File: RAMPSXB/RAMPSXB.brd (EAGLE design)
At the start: 129.5 x 73.5 mm, 97 parts, among them CN1 1X4-BIG, CN2 1X4-BIG, CN3 1X4-BIG, CN4 1X4-BIG, CN5 1X4-BIG, CN6 1X4-BIG, CN7 1X4-BIG, CN8 1X4-BIG, CN9 1X4-BIG, J1 1X2-3.5MM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

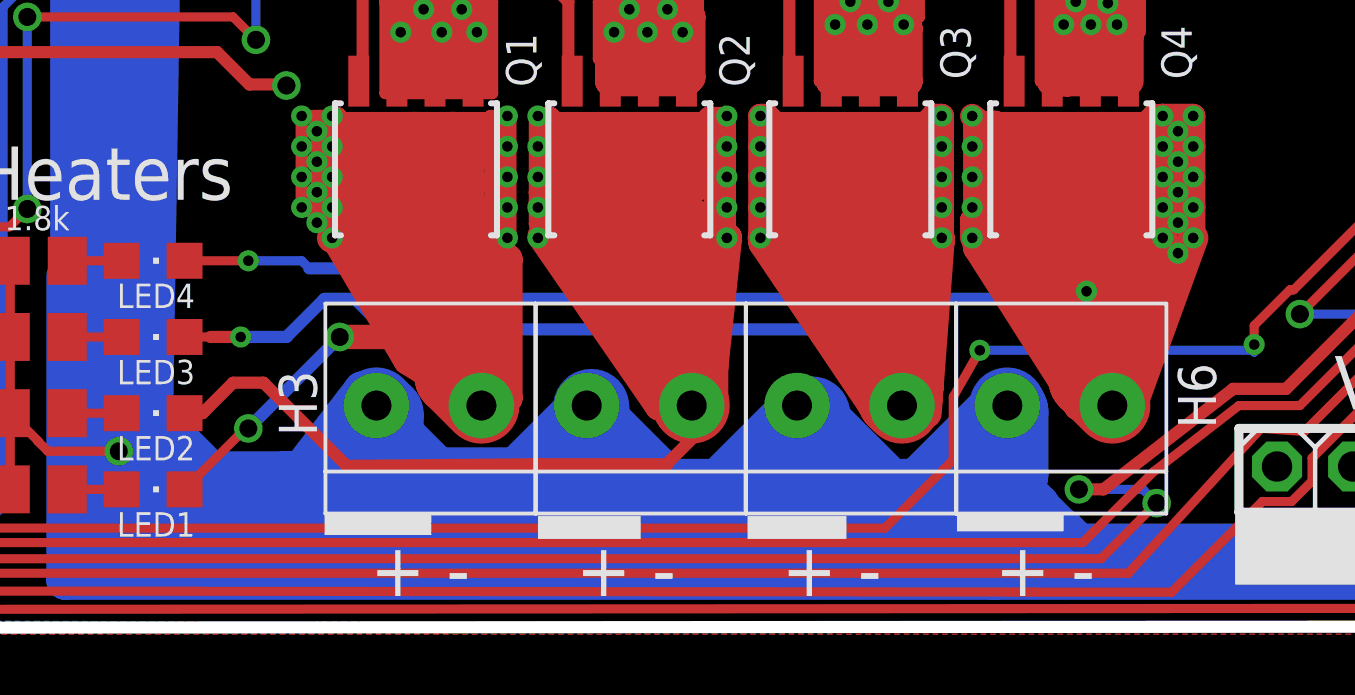
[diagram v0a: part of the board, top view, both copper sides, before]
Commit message: Added Labeling for the Heater LEDs.
So you know which one is which
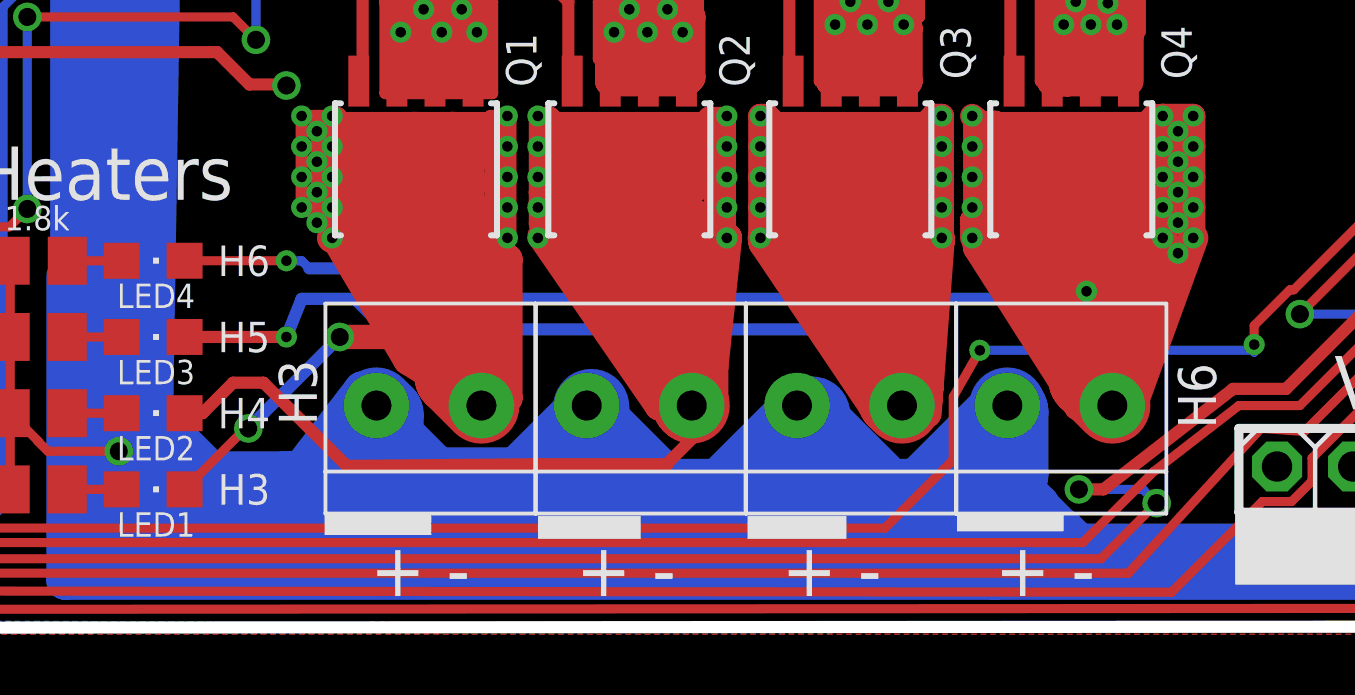
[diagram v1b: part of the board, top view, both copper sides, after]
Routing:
- net N$38: track 125.2 -> 123.6 mm
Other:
- board text added: "H4"
- board text added: "H5"
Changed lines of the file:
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@@
 <layer number="17" name="Pads" color="2" fill="1" visible="yes" active="yes"/>
 <layer number="18" name="Vias" color="2" fill="1" visible="yes" active="yes"/>
-<layer number="19" name="Unrouted" color="13" fill="1" visible="yes" active="yes"/>
+<layer number="19" name="Unrouted" color="13" fill="1" visible="no" active="yes"/>
 <layer number="20" name="Dimension" color="15" fill="1" visible="yes" active="yes"/>
 <layer number="21" name="tPlace" color="7" fill="1" visible="yes" active="yes"/>
@@
 <rectangle x1="1.9304" y1="50.292" x2="19.7104" y2="52.832" layer="21"/>
 <wire x1="22.352" y1="12.954" x2="22.606" y2="13.208" width="0.3048" layer="20"/>
-<text x="41.402" y="5.588" size="1.27" layer="21" font="vector" rot="R90">H3</text>
+<text x="40.132" y="8.128" size="1.27" layer="21" font="vector" rot="R270">H3</text>
 <text x="71.374" y="5.842" size="1.27" layer="21" font="vector" rot="R90">H6</text>
 <text x="13.3604" y="42.672" size="0.8128" layer="21" font="vector">+5V</text>
@@
 <text x="77.978" y="25.654" size="1.016" layer="21" font="vector">(C) Scott Ziv</text>
 <rectangle x1="42.5704" y1="63.5" x2="45.974" y2="70.9168" layer="21"/>
+<text x="38.1" y="3.302" size="1.016" layer="21" font="vector">H3</text>
+<text x="38.1" y="5.842" size="1.016" layer="21" font="vector">H4</text>
+<text x="38.1" y="8.382" size="1.016" layer="21" font="vector">H5</text>
+<text x="38.1" y="10.922" size="1.016" layer="21" font="vector">H6</text>
 </plain>
 <attributes>
@@
 <contactref element="J4" pad="1"/>
 <contactref element="LED3" pad="C"/>
-<wire x1="36.991" y1="8.89" x2="37.846" y2="8.89" width="0.3048" layer="1"/>
+<wire x1="36.991" y1="8.89" x2="37.338" y2="8.89" width="0.3048" layer="1"/>
 <contactref element="Q3" pad="5"/>
 <wire x1="59.182" y1="13.378" x2="59.182" y2="11.176" width="2.54" layer="1"/>
@@
 <wire x1="60.68339375" y1="6.82640625" x2="60.68339375" y2="9.19128125" width="2.54" layer="1"/>
 <wire x1="60.9058" y1="6.604" x2="60.68339375" y2="6.82640625" width="2.54" layer="1"/>
-<wire x1="37.846" y1="8.89" x2="38.862" y2="8.89" width="0.4064" layer="1"/>
-<via x="38.862" y="8.89" extent="1-16" drill="0.35"/>
-<wire x1="38.862" y1="8.89" x2="40.386" y2="8.89" width="0.4064" layer="16"/>
-<wire x1="40.386" y1="8.89" x2="41.656" y2="10.16" width="0.4064" layer="16"/>
-<wire x1="41.656" y1="10.16" x2="42.672" y2="10.16" width="0.4064" layer="16"/>
+<wire x1="37.338" y1="8.89" x2="40.386" y2="8.89" width="0.4064" layer="1"/>
+<via x="40.386" y="8.89" extent="1-16" drill="0.35"/>
+<wire x1="40.386" y1="8.89" x2="40.894" y2="10.16" width="0.4064" layer="16"/>
+<wire x1="40.894" y1="10.16" x2="42.672" y2="10.16" width="0.4064" layer="16"/>
 <wire x1="42.672" y1="10.16" x2="43.688" y2="9.144" width="0.4064" layer="16"/>
 <wire x1="59.436" y1="9.144" x2="60.198" y2="8.382" width="0.4064" layer="16"/>
@@
 <wire x1="69.596" y1="13.208" x2="68.326" y2="12.954" width="0.8128" layer="1"/>
 <wire x1="68.072" y1="13.716" x2="69.596" y2="13.208" width="0.8128" layer="1"/>
-<wire x1="68.072" y1="13.716" x2="69.596" y2="13.208" width="0.8128" layer="1"/>
 <wire x1="69.266928125" y1="14.114309375" x2="69.596" y2="14.224" width="0.8128" layer="1"/>
 <wire x1="69.266928125" y1="14.114309375" x2="68.072" y2="13.716" width="0.8128" layer="1"/>
@@
 <wire x1="68.58" y1="10.922" x2="67.818" y2="10.16" width="1.016" layer="1"/>
 <wire x1="67.818" y1="10.16" x2="67.056" y2="10.414" width="1.016" layer="1"/>
-<wire x1="36.991" y1="11.43" x2="39.116" y2="11.43" width="0.3048" layer="1"/>
-<via x="39.116" y="11.43" extent="1-16" drill="0.35"/>
-<wire x1="39.116" y1="11.43" x2="40.894" y2="11.43" width="0.3048" layer="16"/>
+<wire x1="36.991" y1="11.43" x2="40.386" y2="11.43" width="0.3048" layer="1"/>
+<via x="40.386" y="11.43" extent="1-16" drill="0.35"/>
+<wire x1="40.386" y1="11.43" x2="40.894" y2="11.43" width="0.3048" layer="16"/>
 <wire x1="40.894" y1="11.43" x2="41.148" y2="11.176" width="0.3048" layer="16"/>
 </signal>

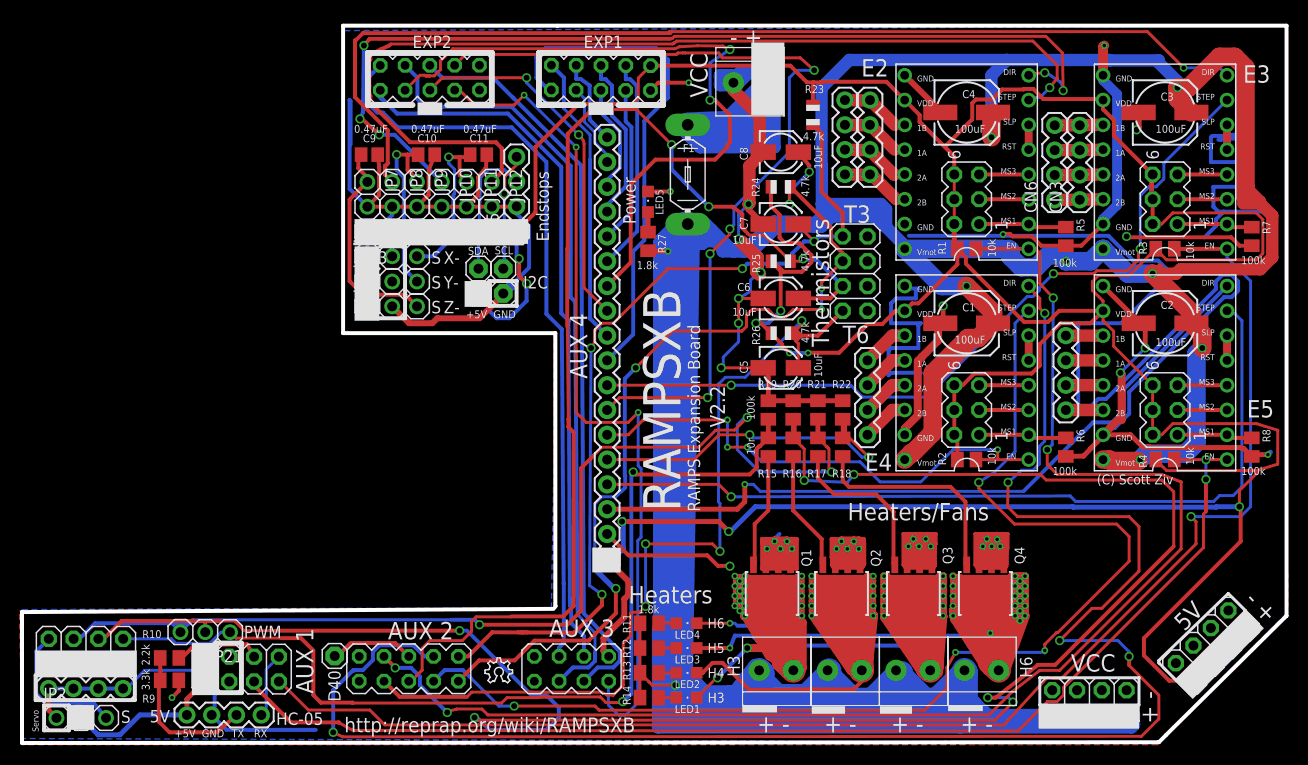
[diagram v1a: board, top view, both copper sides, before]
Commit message: Incremented Version number and added a bigger OSHW Logo to fill in the empty space
Hopefully, this should be close to the final version
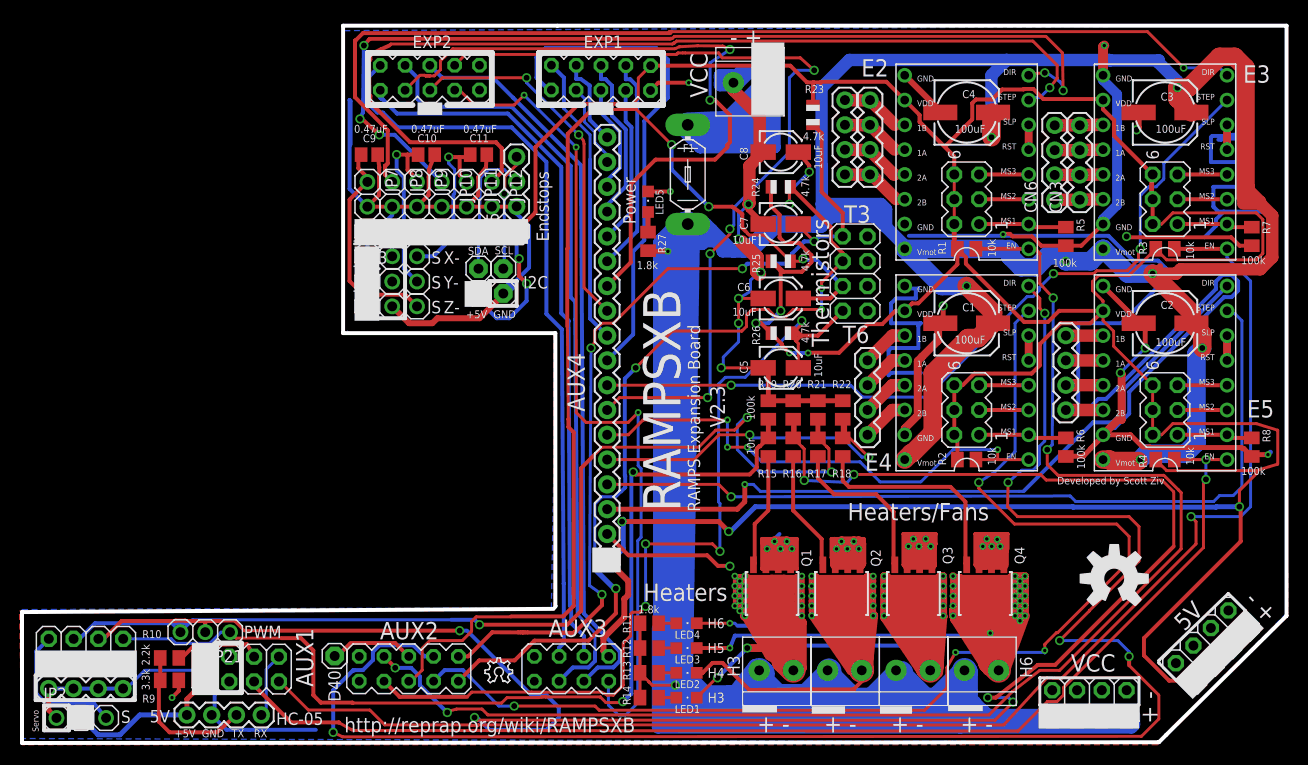
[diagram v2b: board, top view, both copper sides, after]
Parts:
- added LOGO2: OSHW-LOGOL, SparkFun-Aesthetics:OSHW-LOGO-L
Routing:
- net D42: track 174.2 -> 173.6 mm
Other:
- board text added: "AUX1"
- board text added: "AUX2"
- board text added: "AUX3"
- board text added: "AUX4"
- board text added: "Developed by Scott Ziv"
- board text added: "V2.3"
- board text removed: "(C) Scott Ziv"
- board text removed: "AUX 1"
- board text removed: "AUX 2"
- board text removed: "AUX 3"
- board text removed: "AUX 4"
- board text removed: "V2.2"
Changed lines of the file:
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@@
 <layer number="112" name="tSilk" color="15" fill="1" visible="yes" active="yes"/>
 <layer number="113" name="ReferenceLS" color="7" fill="1" visible="no" active="no"/>
+<layer number="114" name="Badge_Outline" color="7" fill="1" visible="no" active="yes"/>
+<layer number="115" name="ReferenceISLANDS" color="7" fill="1" visible="no" active="yes"/>
 <layer number="116" name="centerDrill" color="9" fill="1" visible="yes" active="yes"/>
 <layer number="118" name="Rect_Pads" color="7" fill="1" visible="no" active="no"/>
@@
 <text x="92.964" y="66.802" size="1.778" layer="21" font="vector">E3</text>
 <text x="54.229" y="27.051" size="1.778" layer="21" font="vector">E4</text>
-<text x="93.345" y="32.512" size="1.778" layer="21" font="vector">E5</text>
+<text x="96.139" y="34.29" size="1.778" layer="21" font="vector" rot="R180">E5</text>
 <text x="50.546" y="39.751" size="1.778" layer="21" font="vector" rot="R90">Thermistors</text>
 <text x="66.929" y="23.749" size="1.778" layer="21" font="vector" rot="R180">Heaters/Fans</text>
 <text x="38.1" y="65.278" size="1.778" layer="21" font="vector" rot="R90">VCC</text>
-<text x="38.608" y="15.24" size="1.778" layer="21" font="vector" rot="R180">Heaters</text>
-<text x="12.065" y="11.557" size="1.778" layer="21" font="vector" rot="R180">AUX 2</text>
-<text x="28.575" y="11.811" size="1.778" layer="21" font="vector" rot="R180">AUX 3</text>
-<text x="24.003" y="43.18" size="1.778" layer="21" font="vector" rot="R270">AUX 4</text>
+<text x="40.132" y="15.494" size="1.778" layer="21" font="vector" rot="R180">Heaters</text>
+<text x="10.541" y="11.557" size="1.778" layer="21" font="vector" rot="R180">AUX2</text>
+<text x="27.813" y="11.811" size="1.778" layer="21" font="vector" rot="R180">AUX3</text>
+<text x="23.749" y="39.116" size="1.778" layer="21" font="vector" rot="R270">AUX4</text>
 <text x="84.201" y="1.143" size="1.778" layer="21" font="vector" rot="R90">+ -</text>
 <text x="79.883" y="8.255" size="1.778" layer="21" font="vector" rot="R180">VCC</text>
@@
 <text x="19.2024" y="45.72" size="1.27" layer="21" font="vector">I2C</text>
 <text x="35.306" y="22.86" size="3.81" layer="21" font="vector" rot="R90">RAMPSXB</text>
-<text x="39.878" y="31.496" size="1.524" layer="21" font="vector" rot="R90">V2.2</text>
+<text x="39.878" y="31.496" size="1.524" layer="21" font="vector" rot="R90">V2.3</text>
 <text x="37.338" y="22.86" size="1.27" layer="21" font="vector" rot="R90">RAMPS Expansion Board</text>
 <rectangle x1="-27.2796" y1="0.508" x2="-24.7396" y2="3.048" layer="21"/>
@@
 <rectangle x1="-30.7848" y1="6.096" x2="-20.3708" y2="8.636" layer="21"/>
 <text x="-0.762" y="6.604" size="1.27" layer="21" font="vector" rot="R270">D40</text>
-<text x="-4.064" y="10.922" size="1.778" layer="21" font="vector" rot="R270">AUX 1</text>
+<text x="-4.064" y="10.922" size="1.778" layer="21" font="vector" rot="R270">AUX1</text>
 <wire x1="7.112" y1="50.546" x2="7.112" y2="42.926" width="0.3048" layer="21"/>
 <text x="21.844" y="50.546" size="1.27" layer="21" font="vector" rot="R90">Endstops</text>
@@
 <text x="95.758" y="29.972" size="0.8128" layer="21" font="vector" rot="R90">R8</text>
 <text x="95.25" y="27.432" size="0.8128" layer="21" font="vector" rot="R180">100k</text>
-<text x="75.946" y="27.432" size="0.8128" layer="21" font="vector" rot="R180">100k</text>
+<text x="75.946" y="29.718" size="0.8128" layer="21" font="vector" rot="R270">100k</text>
 <text x="75.946" y="48.768" size="0.8128" layer="21" font="vector" rot="R180">100k</text>
 <text x="95.25" y="49.022" size="0.8128" layer="21" font="vector" rot="R180">100k</text>
@@
 <text x="56.896" y="0.254" size="1.778" layer="21" font="vector">+ -</text>
 <text x="64.008" y="0.254" size="1.778" layer="21" font="vector">+ -</text>
-<text x="77.978" y="25.654" size="1.016" layer="21" font="vector">(C) Scott Ziv</text>
+<text x="73.914" y="25.654" size="0.762" layer="21" font="vector">Developed by Scott Ziv</text>
 <rectangle x1="42.5704" y1="63.5" x2="45.974" y2="70.9168" layer="21"/>
 <text x="38.1" y="3.302" size="1.016" layer="21" font="vector">H3</text>
@@
 <attribute name="NAME" x="69.54868125" y="19.268509375" size="1.01623125" layer="25" font="vector" ratio="18" rot="R270"/>
 </element>
+<element name="LOGO2" library="SparkFun-Aesthetics" package="OSHW-LOGO-L" value="OSHW-LOGOL" x="79.756" y="16.002"/>
 </elements>
 <signals>
@@
 <wire x1="72.136" y1="6.604" x2="74.168" y2="6.604" width="0.3048" layer="1"/>
 <wire x1="74.168" y1="6.604" x2="86.614" y2="19.05" width="0.3048" layer="1"/>
-<wire x1="86.614" y1="25.908" x2="86.614" y2="19.05" width="0.3048" layer="1"/>
 <via x="72.898" y="29.21" extent="1-16" drill="0.6"/>
+<wire x1="86.614" y1="24.807371875" x2="86.614" y2="19.05" width="0.3048" layer="1"/>
 <wire x1="72.898" y1="27.686" x2="72.898" y2="29.21" width="0.3048" layer="1"/>
 <wire x1="72.898" y1="29.21" x2="73.406" y2="29.718" width="0.3048" layer="16"/>
@@
 <wire x1="11.4958625" y1="2.286" x2="11.43" y2="2.286" width="0.3048" layer="1"/>
 <via x="11.43" y="2.286" extent="1-16" drill="0.6"/>
-<wire x1="84.5692" y1="26.6828" x2="86.614" y2="25.908" width="0.3048" layer="1"/>
 <wire x1="14.986" y1="2.6416" x2="15.5908" y2="2.0368" width="0.3048" layer="1"/>
-<wire x1="72.898" y1="27.686" x2="73.914" y2="26.67" width="0.3048" layer="1"/>
 <wire x1="8.6288" y1="5.96326875" x2="8.6288" y2="5.0872" width="0.4064" layer="16"/>
 <wire x1="6.096" y1="6.858" x2="7.73406875" y2="6.858" width="0.4064" layer="16"/>
@@
 <wire x1="66.930146875" y1="2.0368" x2="69.3037125" y2="4.410365625" width="0.3048" layer="1"/>
 <wire x1="15.5908" y1="2.0368" x2="66.930146875" y2="2.0368" width="0.3048" layer="1"/>
-<wire x1="84.582" y1="26.67" x2="84.5692" y2="26.6828" width="0.3048" layer="1" curve="-90"/>
-<wire x1="73.914" y1="26.67" x2="84.582" y2="26.67" width="0.3048" layer="1"/>
+<wire x1="74.0028" y1="26.5812" x2="84.8453" y2="26.5812" width="0.3048" layer="1"/>
+<wire x1="74.0028" y1="26.5812" x2="72.898" y2="27.686" width="0.3048" layer="1"/>
+<wire x1="86.3346" y1="25.0919" x2="86.3346" y2="25.086771875" width="0.3048" layer="1"/>
+<wire x1="86.3346" y1="25.086771875" x2="86.614" y2="24.807371875" width="0.3048" layer="1"/>
+<wire x1="84.8453" y1="26.5812" x2="86.3346" y2="25.0919" width="0.3048" layer="1"/>
 </signal>
 <signal name="D40">
@@
 <wire x1="80.1366875" y1="9.652" x2="74.168" y2="9.652" width="0.3048" layer="16"/>
 <via x="74.168" y="9.652" extent="1-16" drill="0.6"/>
-<wire x1="74.168" y1="9.652" x2="77.47" y2="12.954" width="0.3048" layer="1"/>
-<wire x1="78.486" y1="12.954" x2="82.296" y2="16.764" width="0.3048" layer="1"/>
-<wire x1="82.296" y1="16.764" x2="82.296" y2="21.336" width="0.3048" layer="1"/>
-<wire x1="77.47" y1="12.954" x2="78.486" y2="12.954" width="0.3048" layer="1"/>
+<wire x1="74.168" y1="9.652" x2="77.216" y2="12.7" width="0.3048" layer="1"/>
+<wire x1="82.296" y1="17.803121875" x2="82.296" y2="21.336" width="0.3048" layer="1"/>
 <wire x1="82.296" y1="21.336" x2="81.28" y2="22.352" width="0.3048" layer="1"/>
 <wire x1="81.28" y1="22.352" x2="69.85" y2="22.352" width="0.3048" layer="1"/>
@@
 <wire x1="2.794" y1="6.6286" x2="3.8172" y2="7.6518" width="0.4064" layer="16"/>
 <wire x1="3.8172" y1="7.6518" x2="3.8172" y2="8.50326875" width="0.4064" layer="16"/>
+<wire x1="77.216" y1="12.7" x2="77.216" y2="12.723121875" width="0.3048" layer="1"/>
+<wire x1="77.216" y1="12.723121875" x2="82.296" y2="17.803121875" width="0.3048" layer="1"/>
 </signal>
 <signal name="A11">
@@
 <contactref element="R4" pad="2"/>
 <wire x1="0.34966875" y1="1.24470625" x2="1.645175" y2="0.508" width="0.3048" layer="1"/>
-<wire x1="88.9" y1="22.606" x2="88.9" y2="19.17836875" width="0.3048" layer="1"/>
-<wire x1="89.154" y1="22.86" x2="88.9" y2="22.606" width="0.3048" layer="1"/>
 <via x="89.154" y="26.162" extent="1-16" drill="0.6"/>
 <wire x1="89.154" y1="26.162" x2="89.154" y2="28.194" width="0.3048" layer="16"/>
@@
 <wire x1="0.3048" y1="1.2954" x2="0.35549375" y2="1.24470625" width="0.3048" layer="1"/>
 <wire x1="0.35549375" y1="1.24470625" x2="0.34966875" y2="1.24470625" width="0.3048" layer="1"/>
-<wire x1="89.154" y1="26.162" x2="89.154" y2="22.86" width="0.4064" layer="1"/>
 <wire x1="-8.3566" y1="5.461" x2="-8.3566" y2="5.0546" width="0.4064" layer="1"/>
 <wire x1="-8.3566" y1="5.0546" x2="-4.572" y2="1.27" width="0.4064" layer="1"/>
@@
 <wire x1="72.91793125" y1="3.407703125" x2="69.8921375" y2="0.381909375" width="0.3048" layer="1"/>
 <wire x1="74.5744" y1="4.85276875" x2="74.5744" y2="4.08803125" width="0.3048" layer="1"/>
-<wire x1="88.9" y1="19.17836875" x2="74.5744" y2="4.85276875" width="0.3048" layer="1"/>
+<wire x1="74.5744" y1="4.85276875" x2="88.9" y2="19.17836875" width="0.3048" layer="1"/>
+<wire x1="88.9" y1="19.17836875" x2="88.9" y2="25.908" width="0.3048" layer="1"/>
+<wire x1="88.9" y1="25.908" x2="89.154" y2="26.162" width="0.3048" layer="1"/>
 </signal>
 <signal name="D58">

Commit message: Fixed some issues with V2.1, and updated gerbers
fixed some stuff with V2.1 and corrected some issues
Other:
- board text added: "Developed by S.Z."
- board text removed: "Developed by Scott Ziv"
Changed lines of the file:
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@@
 <text x="56.896" y="0.254" size="1.778" layer="21" font="vector">+ -</text>
 <text x="64.008" y="0.254" size="1.778" layer="21" font="vector">+ -</text>
-<text x="73.914" y="25.654" size="0.762" layer="21" font="vector">Developed by Scott Ziv</text>
+<text x="56.134" y="42.164" size="0.889" layer="21" font="vector" rot="R270">Developed by S.Z.</text>
 <rectangle x1="42.5704" y1="63.5" x2="45.974" y2="70.9168" layer="21"/>
 <text x="38.1" y="3.302" size="1.016" layer="21" font="vector">H3</text>
